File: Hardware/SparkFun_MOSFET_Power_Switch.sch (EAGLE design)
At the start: 31 parts, among them J3 5.5x2.1mm Barrel, Q1 600mA/40V, Q2 100A/100V/6.8mΩ, U1 LMR14203

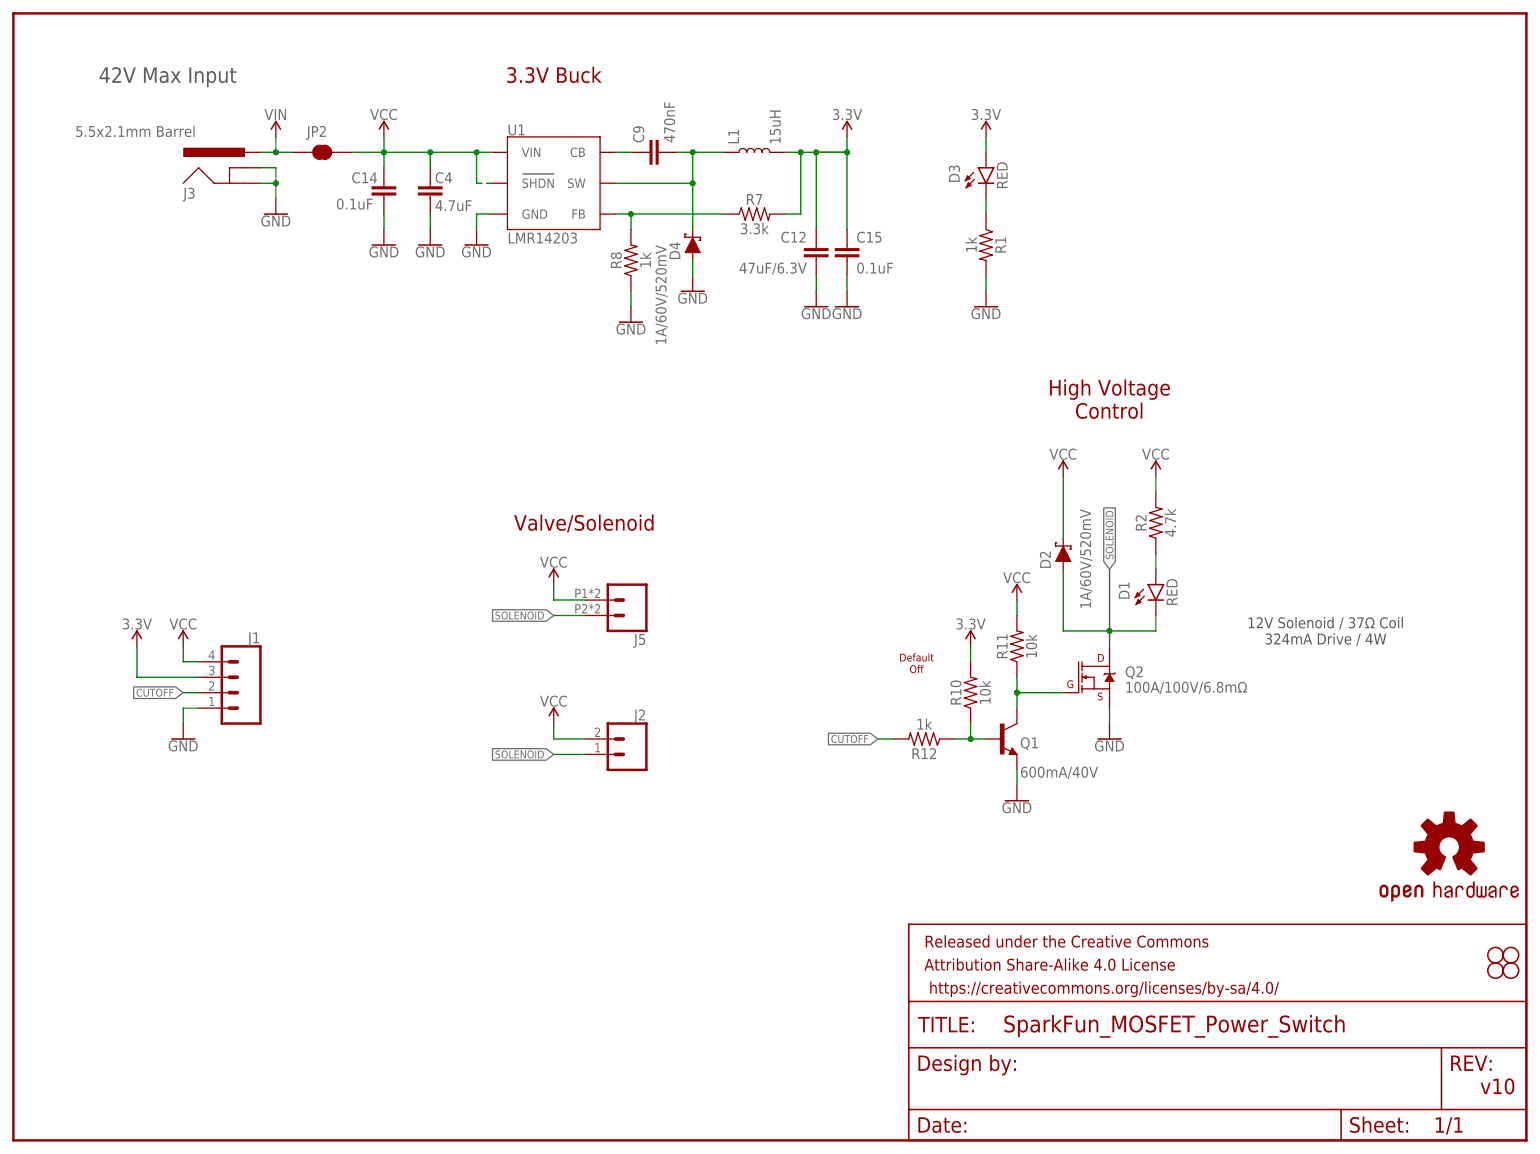
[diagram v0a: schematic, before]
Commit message: add 4-pin female header
-added SMD vertical 4-pin header to allow solderless connection access to the CTRL line and more.
-Added jumpers to kill power and on LEDs
-updated silk to inverted buzzard style
-changed logo to SFE
-updated measures.
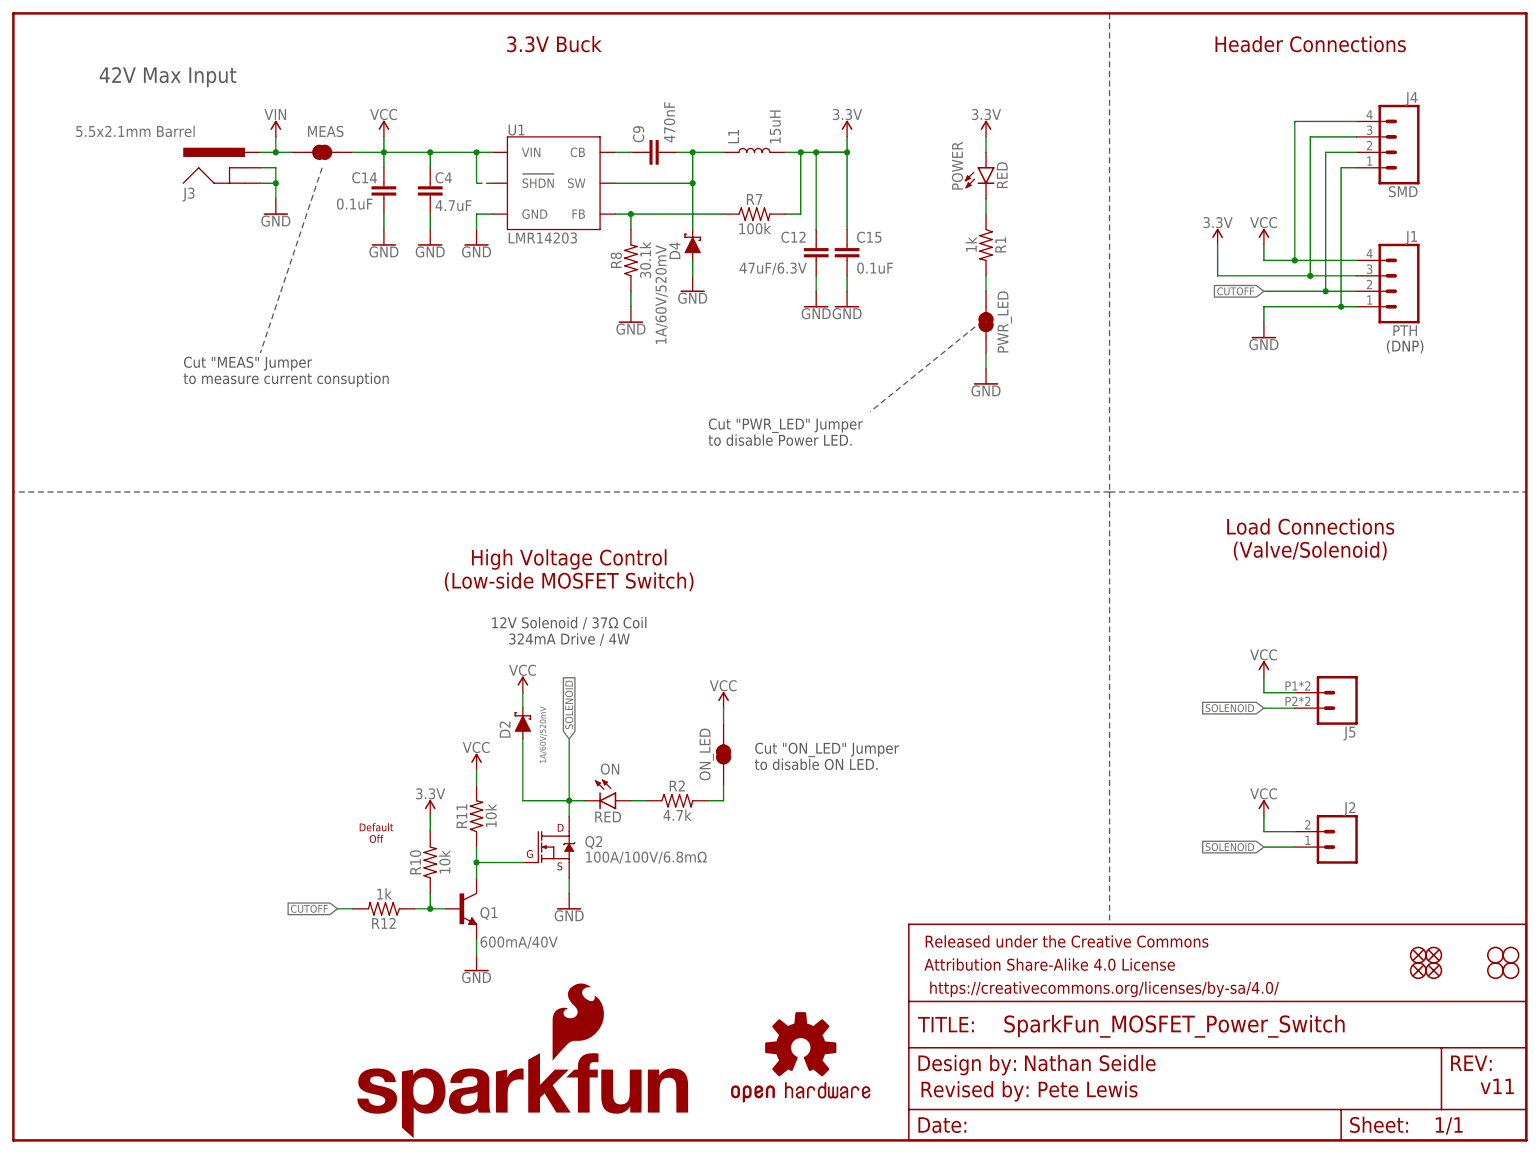
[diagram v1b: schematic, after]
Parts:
- removed D1: RED, SparkFun-LED:LED-RED0603
- added FD1, FD2, FD3, FD4: FIDUCIALUFIDUCIAL, SparkFun-Aesthetics:FIDUCIALUFIDUCIAL
- added J4: SMD, SparkFun-Connectors:CONN_04SMD_STRAIGHT_COMBO
- added LOGO2: SFE_LOGO_NAME_FLAME.1_INCH, SparkFun-Aesthetics:SFE_LOGO_NAME_FLAME.1_INCH
- added ON: RED, SparkFun-LED:LED-RED0603
- added ON_LED, PWR_LED: JUMPER-SMT_2_NC_TRACE_SILK, SparkFun-Jumpers:JUMPER-SMT_2_NC_TRACE_SILK
- J1: value (none) -> PTH
- R7: value 3.3k -> 100k; device SparkFun-Resistors:3.3KOHM-0603-1/10W-1% -> SparkFun-Resistors:100KOHM-0603-1/10W-1%
- R8: value 1k -> 30.1k; device SparkFun-Resistors:1KOHM-0603-1/10W-1% -> SparkFun-Resistors:30.1KOHM-0603-1/10W-1%
- renumbered D3 to POWER, JP2 to MEAS
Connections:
- new net N$6: PWR_LED.2, R1.2
- new net N$7: ON_LED.1, R2.2
- net 3.3V: now also J4.3
- net CUTOFF: now also J4.2
- net GND: now also J4.1, PWR_LED.1; no longer R1.2
- net N$2: now also ON.A; no longer D1.A
- net SOLENOID: now also ON.C; no longer D1.C
- net VCC: now also J4.4, ON_LED.2; no longer R2.2
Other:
- note added: "(DNP)"
- note added: "Cut "MEAS" Jumper to measure current consuption"
- note added: "Cut "ON_LED" Jumper to disable ON LED."
- note added: "Cut "PWR_LED" Jumper to disable Power LED."
- note added: "Header Connections"
- note added: "High Voltage Control (Low-side MOSFET Switch)"
- note added: "Load Connections (Valve/Solenoid)"
- note added: "Nathan Seidle"
- note added: "Revised by: Pete Lewis"
- note added: "v11"
- note removed: "High Voltage Control"
- note removed: "Valve/Solenoid"
- note removed: "v10"
- moved on the sheet: D2, J1, Q1, Q2, R10, R11, R12, R2

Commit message: Buck reg routing
-optimized buck reg routing
-added PTH header for VIN/GND
-added "low-side" to silk name top and bottom
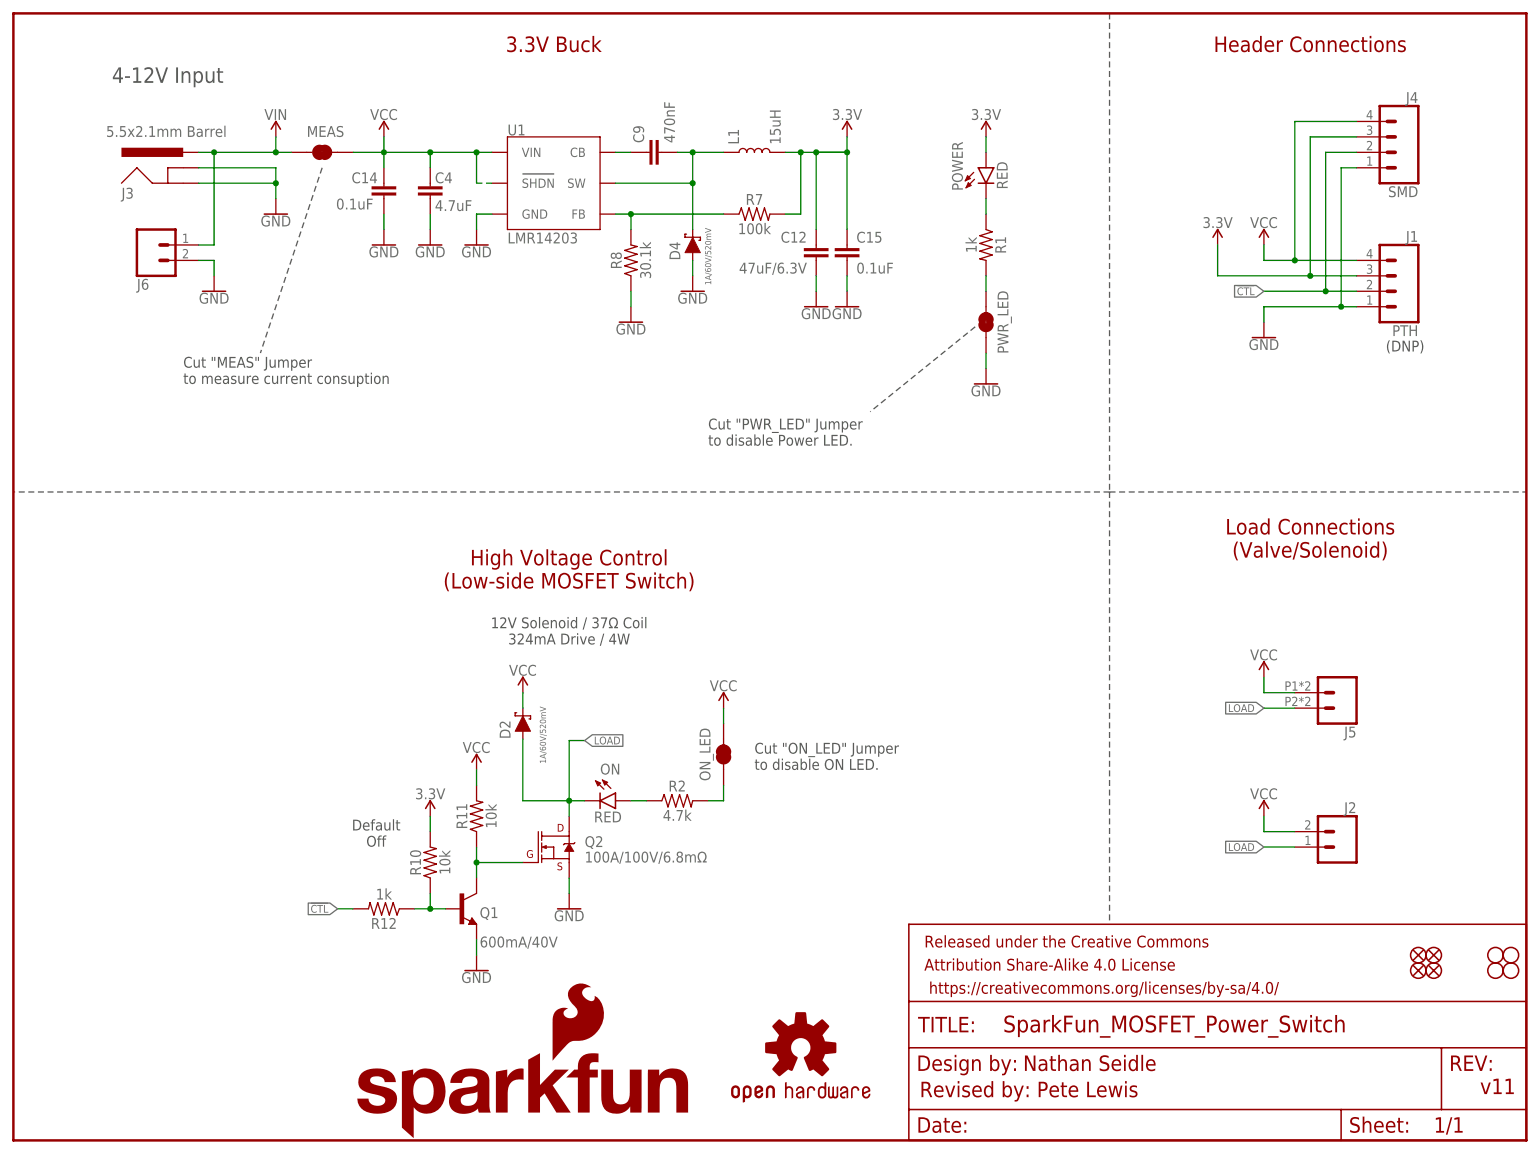
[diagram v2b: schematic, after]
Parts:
- added J6: (no value), SparkFun-Connectors:CONN_021X02_NO_SILK
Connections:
- net CUTOFF renamed !CTL
- net SOLENOID renamed LOAD
- net GND: now also J6.2
- net VIN: now also J6.1
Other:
- note added: "4-12V Input"
- note removed: "42V Max Input"
- moved on the sheet: J3
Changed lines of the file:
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@@
 <part name="FD3" library="SparkFun-Aesthetics" deviceset="FIDUCIAL" device="UFIDUCIAL"/>
 <part name="FD4" library="SparkFun-Aesthetics" deviceset="FIDUCIAL" device="UFIDUCIAL"/>
+<part name="J6" library="SparkFun-Connectors" deviceset="CONN_02" device="1X02_NO_SILK"/>
+<part name="GND3" library="SparkFun-PowerSymbols" deviceset="GND" device=""/>
 </parts>
 <sheets>
@@
 <plain>
 <text x="241.3" y="7.62" size="2.54" layer="94" font="vector">v11</text>
-<text x="59.69" y="50.546" size="1.27" layer="94" font="vector" align="center">Default
+<text x="59.69" y="50.546" size="1.778" layer="97" font="vector" align="center">Default
 Off</text>
 <text x="213.36" y="99.06" size="2.54" layer="94" font="vector" align="center">Load Connections
@@
 324mA Drive / 4W
 </text>
-<text x="25.4" y="175.26" size="2.54" layer="97" font="vector" align="center">42V Max Input</text>
+<text x="25.4" y="175.26" size="2.54" layer="97" font="vector" align="center">4-12V Input</text>
 <text x="166.116" y="11.43" size="2.54" layer="94" font="vector">Nathan Seidle</text>
 <text x="149.098" y="7.112" size="2.54" layer="94" font="vector">Revised by: Pete Lewis</text>
@@
 <instance part="D4" gate="G$1" x="111.76" y="147.32" smashed="yes" rot="R90">
 <attribute name="NAME" x="109.728" y="144.78" size="1.778" layer="95" font="vector" rot="R90"/>
-<attribute name="VALUE" x="105.664" y="130.81" size="1.778" layer="96" font="vector" rot="R90" align="top-left"/>
+<attribute name="VALUE" x="113.792" y="140.716" size="1.016" layer="96" font="vector" rot="R90" align="top-left"/>
 </instance>
 <instance part="GND20" gate="1" x="68.58" y="147.32" smashed="yes" rot="MR0">
@@
 <attribute name="VALUE" x="43.18" y="152.146" size="1.778" layer="96" font="vector" align="top-center"/>
 </instance>
-<instance part="J3" gate="G$1" x="38.1" y="154.94" smashed="yes">
-<attribute name="VALUE" x="10.16" y="165.1" size="1.778" layer="96" font="vector"/>
-<attribute name="NAME" x="27.94" y="154.94" size="1.778" layer="95" font="vector"/>
+<instance part="J3" gate="G$1" x="27.94" y="154.94" smashed="yes">
+<attribute name="VALUE" x="15.24" y="165.1" size="1.778" layer="96" font="vector"/>
+<attribute name="NAME" x="17.78" y="154.94" size="1.778" layer="95" font="vector"/>
 </instance>
 <instance part="J5" gate="J1" x="218.44" y="73.66" smashed="yes" rot="R180">
@@
 <instance part="FD3" gate="G$1" x="231.14" y="27.94" smashed="yes"/>
 <instance part="FD4" gate="G$1" x="233.68" y="27.94" smashed="yes"/>
+<instance part="J6" gate="J1" x="22.86" y="147.32" smashed="yes" rot="MR180">
+<attribute name="VALUE" x="20.32" y="152.146" size="1.778" layer="96" font="vector" rot="MR180"/>
+<attribute name="NAME" x="20.32" y="141.732" size="1.778" layer="95" font="vector" rot="MR180"/>
+</instance>
+<instance part="GND3" gate="1" x="33.02" y="139.7" smashed="yes">
+<attribute name="VALUE" x="33.02" y="139.446" size="1.778" layer="96" font="vector" align="top-center"/>
+</instance>
 </instances>
 <busses>
@@
 </segment>
 <segment>
-<wire x1="40.64" y1="157.48" x2="43.18" y2="157.48" width="0.1524" layer="91"/>
+<wire x1="30.48" y1="157.48" x2="43.18" y2="157.48" width="0.1524" layer="91"/>
 <wire x1="43.18" y1="157.48" x2="43.18" y2="154.94" width="0.1524" layer="91"/>
-<wire x1="40.64" y1="160.02" x2="43.18" y2="160.02" width="0.1524" layer="91"/>
+<wire x1="30.48" y1="160.02" x2="43.18" y2="160.02" width="0.1524" layer="91"/>
 <wire x1="43.18" y1="160.02" x2="43.18" y2="157.48" width="0.1524" layer="91"/>
 <junction x="43.18" y="157.48"/>
@@
 <pinref part="PWR_LED" gate="G$1" pin="1"/>
 </segment>
+<segment>
+<pinref part="J6" gate="J1" pin="2"/>
+<wire x1="30.48" y1="144.78" x2="33.02" y2="144.78" width="0.1524" layer="91"/>
+<pinref part="GND3" gate="1" pin="GND"/>
+<wire x1="33.02" y1="144.78" x2="33.02" y2="142.24" width="0.1524" layer="91"/>
+</segment>
 </net>
 <net name="N$2" class="0">
@@
 <pinref part="ON" gate="G$1" pin="A"/>
 <wire x1="101.6" y1="55.88" x2="104.14" y2="55.88" width="0.1524" layer="91"/>
-</segment>
-</net>
-<net name="CUTOFF" class="0">
-<segment>
-<pinref part="R12" gate="G$1" pin="2"/>
-<wire x1="55.88" y1="38.1" x2="53.34" y2="38.1" width="0.1524" layer="91"/>
-<label x="53.34" y="38.1" size="1.27" layer="95" font="vector" rot="R180" xref="yes"/>
-</segment>
-<segment>
-<pinref part="J1" gate="J1" pin="2"/>
-<wire x1="220.98" y1="139.7" x2="215.9" y2="139.7" width="0.1524" layer="91"/>
-<label x="205.74" y="139.7" size="1.27" layer="95" font="vector" rot="R180" xref="yes"/>
-<wire x1="215.9" y1="139.7" x2="205.74" y2="139.7" width="0.1524" layer="91"/>
-<wire x1="215.9" y1="139.7" x2="215.9" y2="162.56" width="0.1524" layer="91"/>
-<junction x="215.9" y="139.7"/>
-<pinref part="J4" gate="J1" pin="2"/>
-<wire x1="215.9" y1="162.56" x2="220.98" y2="162.56" width="0.1524" layer="91"/>
 </segment>
 </net>
@@
 <wire x1="45.72" y1="162.56" x2="43.18" y2="162.56" width="0.1524" layer="91"/>
 <wire x1="43.18" y1="162.56" x2="43.18" y2="165.1" width="0.1524" layer="91"/>
-<wire x1="40.64" y1="162.56" x2="43.18" y2="162.56" width="0.1524" layer="91"/>
+<wire x1="30.48" y1="162.56" x2="33.02" y2="162.56" width="0.1524" layer="91"/>
 <junction x="43.18" y="162.56"/>
 <pinref part="J3" gate="G$1" pin="PWR"/>
 <pinref part="SUPPLY3" gate="G$1" pin="VIN"/>
 <pinref part="MEAS" gate="JP1" pin="1"/>
-</segment>
-</net>
-<net name="SOLENOID" class="0">
+<wire x1="33.02" y1="162.56" x2="43.18" y2="162.56" width="0.1524" layer="91"/>
+<wire x1="33.02" y1="162.56" x2="33.02" y2="147.32" width="0.1524" layer="91"/>
+<junction x="33.02" y="162.56"/>
+<pinref part="J6" gate="J1" pin="1"/>
+<wire x1="33.02" y1="147.32" x2="30.48" y2="147.32" width="0.1524" layer="91"/>
+</segment>
+</net>
+<net name="LOAD" class="0">
 <segment>
 <wire x1="210.82" y1="71.12" x2="205.74" y2="71.12" width="0.1524" layer="91"/>
@@
 <wire x1="91.44" y1="55.88" x2="93.98" y2="55.88" width="0.1524" layer="91"/>
 <pinref part="ON" gate="G$1" pin="C"/>
-<wire x1="91.44" y1="55.88" x2="91.44" y2="66.04" width="0.1524" layer="91"/>
+<wire x1="91.44" y1="55.88" x2="91.44" y2="65.786" width="0.1524" layer="91"/>
+<wire x1="91.44" y1="65.786" x2="93.98" y2="65.786" width="0.1524" layer="91"/>
 <junction x="91.44" y="55.88"/>
-<label x="91.44" y="66.04" size="1.27" layer="95" font="vector" rot="R90" xref="yes"/>
+<label x="93.98" y="65.786" size="1.27" layer="95" font="vector" xref="yes"/>
 <wire x1="91.44" y1="55.88" x2="83.82" y2="55.88" width="0.1524" layer="91"/>
 <pinref part="D2" gate="G$1" pin="A"/>
@@
 </segment>
 </net>
+<net name="!CTL" class="0">
+<segment>
+<pinref part="R12" gate="G$1" pin="2"/>
+<wire x1="55.88" y1="38.1" x2="53.34" y2="38.1" width="0.1524" layer="91"/>
+<label x="53.34" y="38.1" size="1.27" layer="95" font="vector" rot="R180" xref="yes"/>
+</segment>
+<segment>
+<pinref part="J1" gate="J1" pin="2"/>
+<wire x1="220.98" y1="139.7" x2="215.9" y2="139.7" width="0.1524" layer="91"/>
+<label x="205.74" y="139.7" size="1.27" layer="95" font="vector" rot="R180" xref="yes"/>
+<wire x1="215.9" y1="139.7" x2="205.74" y2="139.7" width="0.1524" layer="91"/>
+<wire x1="215.9" y1="139.7" x2="215.9" y2="162.56" width="0.1524" layer="91"/>
+<junction x="215.9" y="139.7"/>
+<pinref part="J4" gate="J1" pin="2"/>
+<wire x1="215.9" y1="162.56" x2="220.98" y2="162.56" width="0.1524" layer="91"/>
+</segment>
+</net>
